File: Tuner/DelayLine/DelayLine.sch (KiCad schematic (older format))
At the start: 85 parts, among them J1 Conn_Coaxial, J10 Conn_Coaxial, J11 Conn_Coaxial, J12 Conn_Coaxial, J13 Conn_01x01, J14 Conn_01x01, J15 Conn_01x01, J16 Conn_01x01, J17 Conn_02x10_Odd_Even, J18 Conn_Coaxial, J19 Conn_Coaxial, J20 Conn_Coaxial, J21 Conn_Coaxial, J22 Conn_Coaxial, J23 Conn_Coaxial, J24 Conn_01x01, J25 Conn_01x01, J26 Conn_01x01, J27 Conn_01x01, J28 Conn_01x01, J29 Conn_Coaxial, J3 Conn_Coaxial, J31 Conn_Coaxial, J32 Conn_01x01, J33 Conn_01x01, J34 Conn_01x01, J35 Conn_01x01, J5 Conn_Coaxial, J6 Conn_Coaxial, J7 Conn_Coaxial, J8 Conn_01x02, J9 Conn_01x02

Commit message: Stupid mistake, went to another method
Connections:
- net at RLY1.4 (NO), RLY1.8 (NO), RLY2.6 (Pole): no longer J10.1 (In), RLY2.2 (Pole)
- net at RLY2.4 (NO): now also J6.1 (In)
- net at RLY2.8 (NO): now also J10.1 (In)
- net at RLY3.4 (NO): now also J12.1 (In)
- net at RLY3.8 (NO): now also J19.1 (In)
- net at RLY4.4 (NO): now also J21.1 (In)
- net at RLY4.8 (NO): now also J23.1 (In)
- net at RLY5.4 (NO): now also J29.1 (In)
- net at RLY5.8 (NO): now also J31.1 (In)
- net at RLY6.4 (NO): now also J1.1 (In)
- net at RLY6.8 (NO): now also J3.1 (In)
- net at RLY7.4 (NO): now also J5.1 (In)
- net at RLY7.8 (NO): now also J7.1 (In)
- net at RLY8.4 (NO): now also J11.1 (In)
- net at RLY8.8 (NO): now also J18.1 (In)
- net at RLY9.4 (NO): now also J20.1 (In)
- net at RLY9.8 (NO): now also J22.1 (In)
- new net: J24.1 (Pin_1), RLY10.3 (NC), RLY9.2 (Pole)
- new net: RLY2.2 (Pole), RLY3.6 (Pole)
- new net: RLY2.3 (NC), RLY2.7 (NC)
- new net: RLY3.2 (Pole), RLY4.6 (Pole)
- new net: RLY3.3 (NC), RLY3.7 (NC)
- new net: RLY4.2 (Pole), RLY5.6 (Pole)
- new net: RLY4.3 (NC), RLY4.7 (NC)
- new net: RLY5.2 (Pole), RLY6.6 (Pole)
- new net: RLY5.3 (NC), RLY5.7 (NC)
- new net: RLY6.2 (Pole), RLY7.6 (Pole)
- new net: RLY6.3 (NC), RLY6.7 (NC)
- new net: RLY7.2 (Pole), RLY8.6 (Pole)
- new net: RLY7.3 (NC), RLY7.7 (NC)
- new net: RLY8.2 (Pole), RLY9.6 (Pole)
- new net: RLY8.3 (NC), RLY8.7 (NC)
- new net: RLY9.3 (NC), RLY9.7 (NC)
- now unconnected: RLY10.7 (NC)
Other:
- moved on the sheet: J10, J24, J32, J33, J34, J35, J6, J8, J9, RLY1, RLY10, RLY2

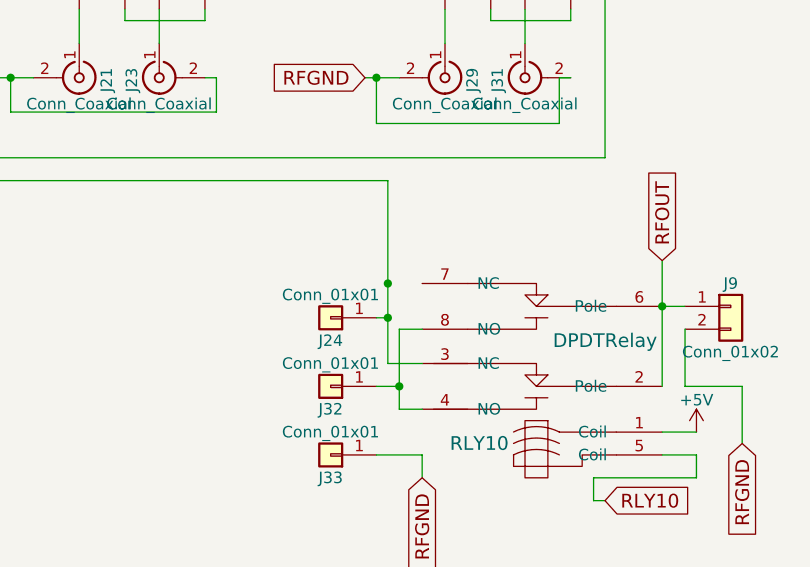
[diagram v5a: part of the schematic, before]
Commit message: Added LittleDelayLine
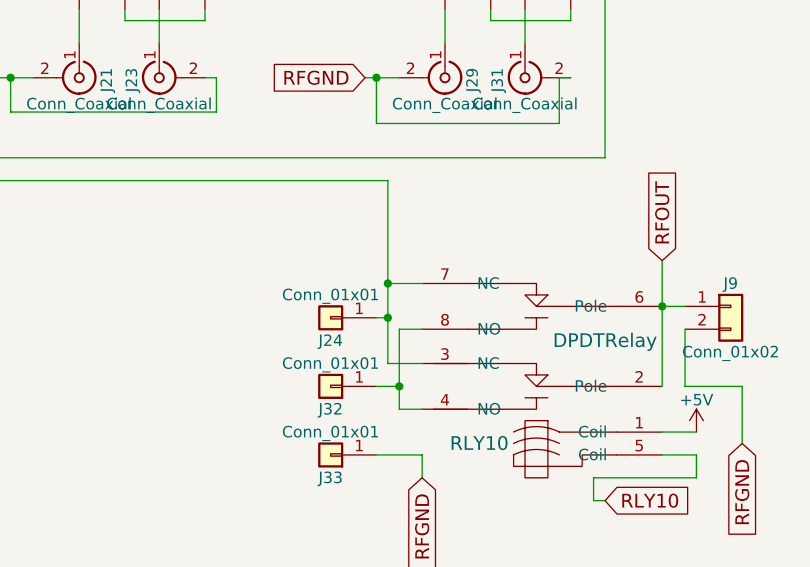
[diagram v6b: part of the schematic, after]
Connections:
- net at J24.1 (Pin_1), RLY10.3 (NC), RLY9.2 (Pole): now also RLY10.7 (NC)
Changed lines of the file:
@@
 Wire Wire Line
 	4250 4150 4250 4000
+Wire Wire Line
+	7450 3150 7600 3150
 $EndSCHEMATC

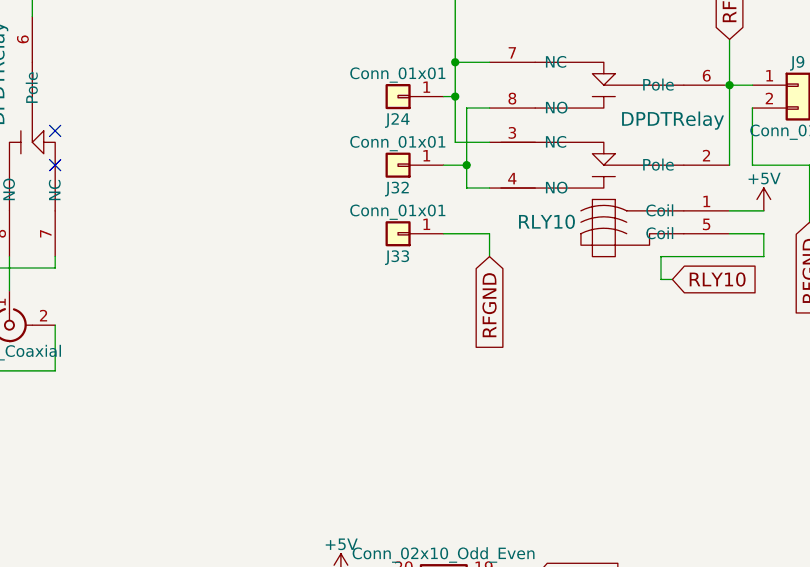
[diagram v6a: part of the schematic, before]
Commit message: Added more instrumentation to TandemMatch, fixed grounding issue
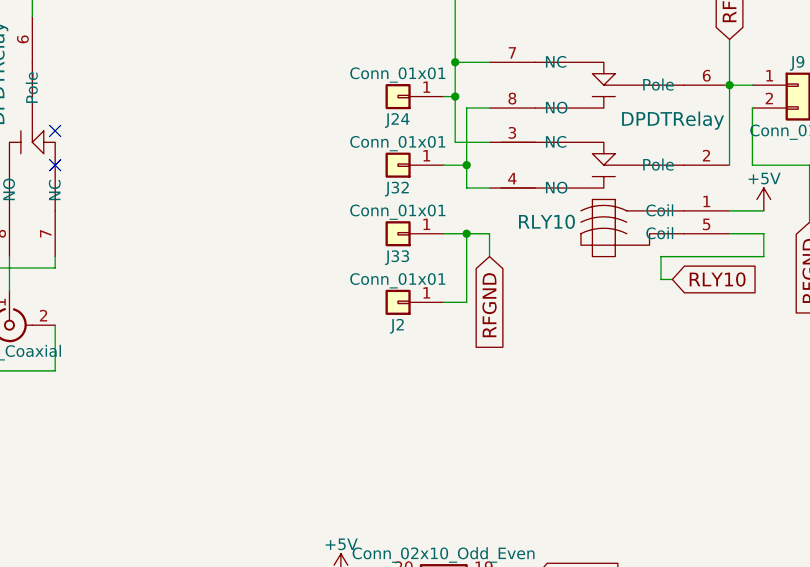
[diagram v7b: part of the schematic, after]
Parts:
- added J2: Conn_01x01, Connectors:1pin, symbol Conn_01x01
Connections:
- net RFGND: now also J2.1 (Pin_1)
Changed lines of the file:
@@
 $EndComp
 $Comp
-L +5V #PWR01
+L +5V #PWR2
 U 1 1 5B1A4DAD
 P 950 1250
-F 0 "#PWR01" H 950 1100 50  0001 C CNN
+F 0 "#PWR2" H 950 1100 50  0001 C CNN
 F 1 "+5V" H 950 1390 50  0000 C CNN
 F 2 "" H 950 1250 50  0001 C CNN
@@
 $EndComp
 $Comp
-L +5V #PWR02
+L +5V #PWR5
 U 1 1 5B25DE9C
 P 1450 6400
-F 0 "#PWR02" H 1450 6250 50  0001 C CNN
+F 0 "#PWR5" H 1450 6250 50  0001 C CNN
 F 1 "+5V" H 1450 6540 50  0000 C CNN
 F 2 "" H 1450 6400 50  0001 C CNN
@@
 $EndComp
 $Comp
-L +5V #PWR03
+L +5V #PWR6
 U 1 1 5B25F712
 P 1800 6400
-F 0 "#PWR03" H 1800 6250 50  0001 C CNN
+F 0 "#PWR6" H 1800 6250 50  0001 C CNN
 F 1 "+5V" H 1800 6540 50  0000 C CNN
 F 2 "" H 1800 6400 50  0001 C CNN
@@
 $EndComp
 $Comp
-L +5V #PWR04
+L +5V #PWR7
 U 1 1 5B25F91B
 P 2150 6400
-F 0 "#PWR04" H 2150 6250 50  0001 C CNN
+F 0 "#PWR7" H 2150 6250 50  0001 C CNN
 F 1 "+5V" H 2150 6540 50  0000 C CNN
 F 2 "" H 2150 6400 50  0001 C CNN
@@
 $EndComp
 $Comp
-L +5V #PWR05
+L +5V #PWR8
 U 1 1 5B25F931
 P 2500 6400
-F 0 "#PWR05" H 2500 6250 50  0001 C CNN
+F 0 "#PWR8" H 2500 6250 50  0001 C CNN
 F 1 "+5V" H 2500 6540 50  0000 C CNN
 F 2 "" H 2500 6400 50  0001 C CNN
@@
 $EndComp
 $Comp
-L +5V #PWR06
+L +5V #PWR10
 U 1 1 5B25FB4D
 P 2800 6400
-F 0 "#PWR06" H 2800 6250 50  0001 C CNN
+F 0 "#PWR10" H 2800 6250 50  0001 C CNN
 F 1 "+5V" H 2800 6540 50  0000 C CNN
 F 2 "" H 2800 6400 50  0001 C CNN
@@
 $EndComp
 $Comp
-L +5V #PWR07
+L +5V #PWR12
 U 1 1 5B25FB63
 P 3150 6400
-F 0 "#PWR07" H 3150 6250 50  0001 C CNN
+F 0 "#PWR12" H 3150 6250 50  0001 C CNN
 F 1 "+5V" H 3150 6540 50  0000 C CNN
 F 2 "" H 3150 6400 50  0001 C CNN
@@
 $EndComp
 $Comp
-L +5V #PWR08
+L +5V #PWR13
 U 1 1 5B25FB79
 P 3500 6400
-F 0 "#PWR08" H 3500 6250 50  0001 C CNN
+F 0 "#PWR13" H 3500 6250 50  0001 C CNN
 F 1 "+5V" H 3500 6540 50  0000 C CNN
 F 2 "" H 3500 6400 50  0001 C CNN
@@
 $EndComp
 $Comp
-L +5V #PWR09
+L +5V #PWR14
 U 1 1 5B25FB8F
 P 3850 6400
-F 0 "#PWR09" H 3850 6250 50  0001 C CNN
+F 0 "#PWR14" H 3850 6250 50  0001 C CNN
 F 1 "+5V" H 3850 6540 50  0000 C CNN
 F 2 "" H 3850 6400 50  0001 C CNN
@@
 RLY10
 $Comp
-L +5V #PWR010
+L +5V #PWR21
 U 1 1 5B89A678
 P 6950 5400
-F 0 "#PWR010" H 6950 5250 50  0001 C CNN
+F 0 "#PWR21" H 6950 5250 50  0001 C CNN
 F 1 "+5V" H 6950 5540 50  0000 C CNN
 F 2 "" H 6950 5400 50  0001 C CNN
@@
 $EndComp
 $Comp
-L +5V #PWR011
+L +5V #PWR3
 U 1 1 5B89BB19
 P 1150 6400
-F 0 "#PWR011" H 1150 6250 50  0001 C CNN
+F 0 "#PWR3" H 1150 6250 50  0001 C CNN
 F 1 "+5V" H 1150 6540 50  0000 C CNN
 F 2 "" H 1150 6400 50  0001 C CNN
@@
 $EndComp
 $Comp
-L +5V #PWR012
+L +5V #PWR1
 U 1 1 5B89BBCB
 P 850 6400
-F 0 "#PWR012" H 850 6250 50  0001 C CNN
+F 0 "#PWR1" H 850 6250 50  0001 C CNN
 F 1 "+5V" H 850 6540 50  0000 C CNN
 F 2 "" H 850 6400 50  0001 C CNN
@@
 RLY9
 $Comp
-L +5V #PWR013
+L +5V #PWR19
 U 1 1 5B89FB34
 P 5750 5650
-F 0 "#PWR013" H 5750 5500 50  0001 C CNN
+F 0 "#PWR19" H 5750 5500 50  0001 C CNN
 F 1 "+5V" H 5750 5790 50  0000 C CNN
 F 2 "" H 5750 5650 50  0001 C CNN
@@
 $EndComp
 $Comp
-L +5V #PWR014
+L +5V #PWR24
 U 1 1 5B97C780
 P 9800 5900
-F 0 "#PWR014" H 9800 5750 50  0001 C CNN
+F 0 "#PWR24" H 9800 5750 50  0001 C CNN
 F 1 "+5V" H 9800 6040 50  0000 C CNN
 F 2 "" H 9800 5900 50  0001 C CNN
@@
 RLY9
 $Comp
-L +5V #PWR015
+L +5V #PWR16
 U 1 1 5BA3849B
 P 4450 5700
-F 0 "#PWR015" H 4450 5550 50  0001 C CNN
+F 0 "#PWR16" H 4450 5550 50  0001 C CNN
 F 1 "+5V" H 4450 5840 50  0000 C CNN
 F 2 "" H 4450 5700 50  0001 C CNN
@@
 RLY2
 $Comp
-L +5V #PWR016
+L +5V #PWR11
 U 1 1 5C733753
 P 2950 900
-F 0 "#PWR016" H 2950 750 50  0001 C CNN
+F 0 "#PWR11" H 2950 750 50  0001 C CNN
 F 1 "+5V" H 2950 1040 50  0000 C CNN
 F 2 "" H 2950 900 50  0001 C CNN
@@
 RLY10
 $Comp
-L +5V #PWR017
+L +5V #PWR23
 U 1 1 5C7350A4
 P 8800 3800
-F 0 "#PWR017" H 8800 3650 50  0001 C CNN
+F 0 "#PWR23" H 8800 3650 50  0001 C CNN
 F 1 "+5V" H 8800 3940 50  0000 C CNN
 F 2 "" H 8800 3800 50  0001 C CNN
@@
 RLY3
 $Comp
-L +5V #PWR018
+L +5V #PWR17
 U 1 1 5C759EA2
 P 4500 900
-F 0 "#PWR018" H 4500 750 50  0001 C CNN
+F 0 "#PWR17" H 4500 750 50  0001 C CNN
 F 1 "+5V" H 4500 1040 50  0000 C CNN
 F 2 "" H 4500 900 50  0001 C CNN
@@
 RLY4
 $Comp
-L +5V #PWR019
+L +5V #PWR20
 U 1 1 5C75A6EF
 P 6100 900
-F 0 "#PWR019" H 6100 750 50  0001 C CNN
+F 0 "#PWR20" H 6100 750 50  0001 C CNN
 F 1 "+5V" H 6100 1040 50  0000 C CNN
 F 2 "" H 6100 900 50  0001 C CNN
@@
 RLY5
 $Comp
-L +5V #PWR020
+L +5V #PWR22
 U 1 1 5C75AF8D
 P 7700 900
-F 0 "#PWR020" H 7700 750 50  0001 C CNN
+F 0 "#PWR22" H 7700 750 50  0001 C CNN
 F 1 "+5V" H 7700 1040 50  0000 C CNN
 F 2 "" H 7700 900 50  0001 C CNN
@@
 RLY6
 $Comp
-L +5V #PWR021
+L +5V #PWR4
 U 1 1 5C75CACE
 P 1450 2950
-F 0 "#PWR021" H 1450 2800 50  0001 C CNN
+F 0 "#PWR4" H 1450 2800 50  0001 C CNN
 F 1 "+5V" H 1450 3090 50  0000 C CNN
 F 2 "" H 1450 2950 50  0001 C CNN
@@
 RLY7
 $Comp
-L +5V #PWR022
+L +5V #PWR9
 U 1 1 5C75D7A5
 P 2650 2950
-F 0 "#PWR022" H 2650 2800 50  0001 C CNN
+F 0 "#PWR9" H 2650 2800 50  0001 C CNN
 F 1 "+5V" H 2650 3090 50  0000 C CNN
 F 2 "" H 2650 2950 50  0001 C CNN
@@
 RLY8
 $Comp
-L +5V #PWR023
+L +5V #PWR15
 U 1 1 5C75E937
 P 3900 2950
-F 0 "#PWR023" H 3900 2800 50  0001 C CNN
+F 0 "#PWR15" H 3900 2800 50  0001 C CNN
 F 1 "+5V" H 3900 3090 50  0000 C CNN
 F 2 "" H 3900 2950 50  0001 C CNN
@@
 RLY9
 $Comp
-L +5V #PWR024
+L +5V #PWR18
 U 1 1 5C75F12E
 P 5150 2950
-F 0 "#PWR024" H 5150 2800 50  0001 C CNN
+F 0 "#PWR18" H 5150 2800 50  0001 C CNN
 F 1 "+5V" H 5150 3090 50  0000 C CNN
 F 2 "" H 5150 2950 50  0001 C CNN
@@
 Wire Wire Line
 	7450 3150 7600 3150
+$Comp
+L Conn_01x01 J2
+U 1 1 5C744B1A
+P 7200 4200
+F 0 "J2" H 7200 4300 50  0000 C CNN
+F 1 "Conn_01x01" H 7200 4100 50  0000 C CNN
+F 2 "Connectors:1pin" H 7200 4200 50  0001 C CNN
+F 3 "" H 7200 4200 50  0001 C CNN
+	1    7200 4200
+	-1   0    0    1
+$EndComp
+Wire Wire Line
+	7400 4200 7500 4200
+Wire Wire Line
+	7500 4200 7500 3900
+Connection ~ 7500 3900
 $EndSCHEMATC

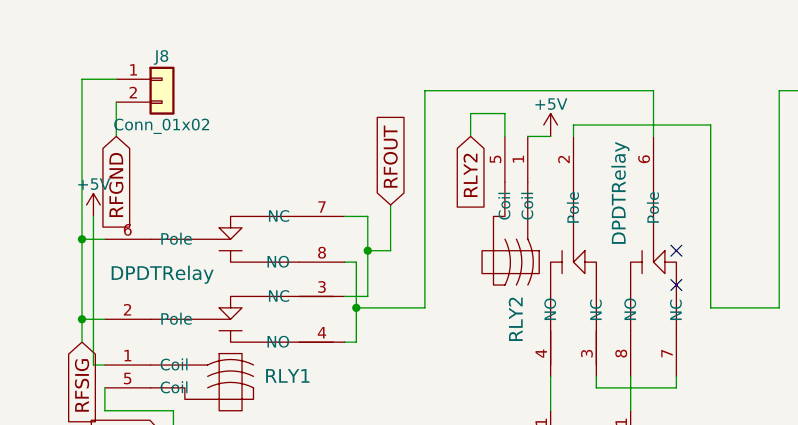
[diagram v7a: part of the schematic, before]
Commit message: Added BNC and screw terminal combo pads
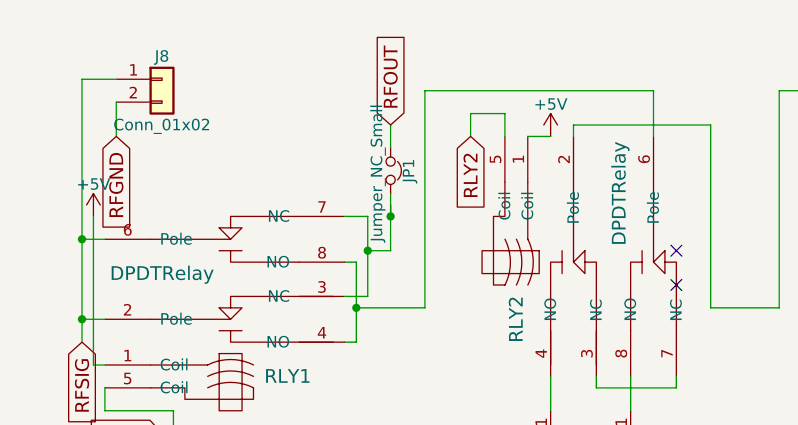
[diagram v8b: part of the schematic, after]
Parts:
- added JP1: Jumper_NC_Small, Pin_Headers:Pin_Header_Straight_1x02_Pitch2.54mm, symbol Jumper_NC_Small
- J8, J9: footprint Connectors_Terminal_Blocks:TerminalBlock_bornier-2_P5.08mm -> tuner:bnc_90_1-1337543-0_pad_combo
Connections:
- net RFOUT: now also JP1.1; no longer RLY1.3 (NC), RLY1.7 (NC)
- new net: JP1.2, RLY1.3 (NC), RLY1.7 (NC)
